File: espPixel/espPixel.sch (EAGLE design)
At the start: 83 parts, among them IC1 74LVC1T45GW,125, IC2 74LVC1T45GW,125, IC3 MP2315GJ-Z, IC4 CP2104, J1 TBLH10-350-04BK, J2 TBLH10-350-03BK, J3 TBLH10-350-02BK, Q1 SIR414DP-T1-GE3, Q2 SIR414DP-T1-GE3, Q5 mmbt2222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

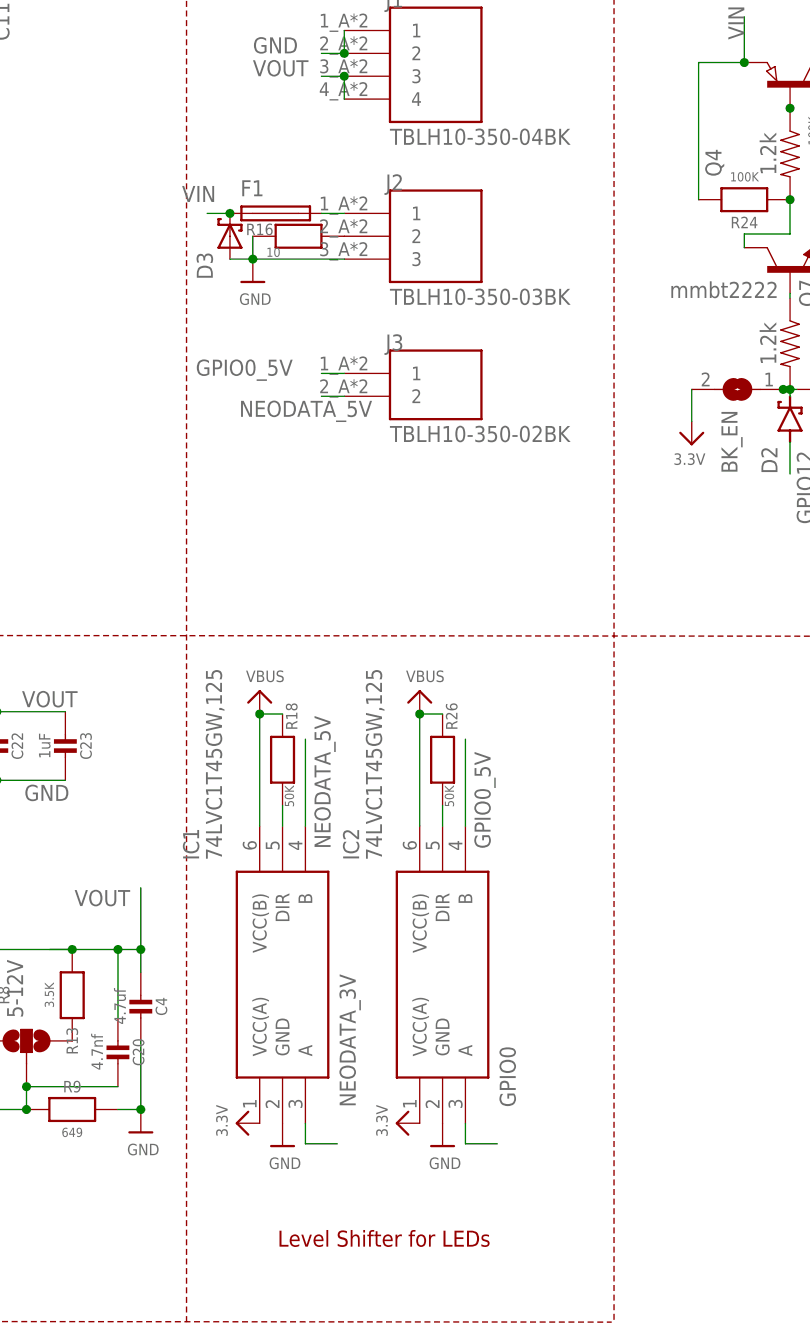
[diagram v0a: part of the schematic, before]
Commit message: v3 more compact size
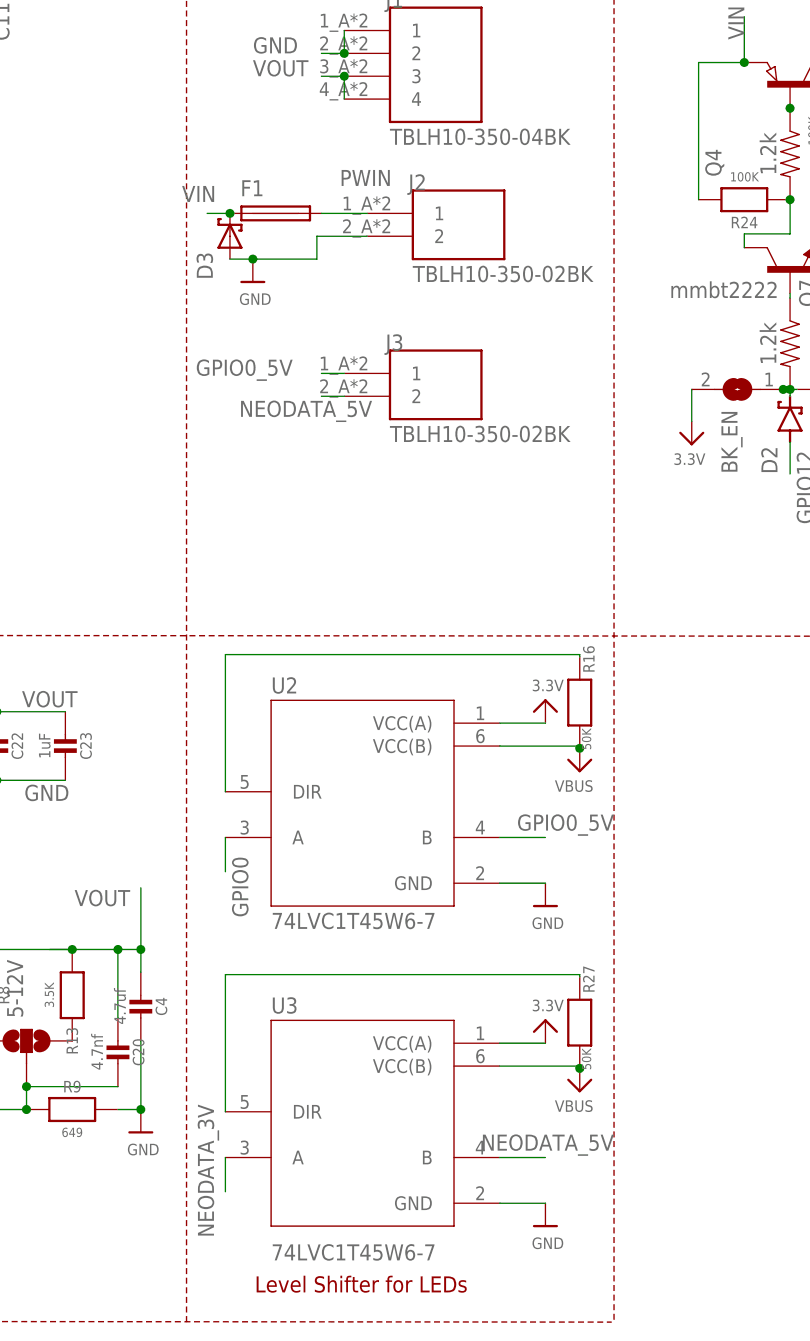
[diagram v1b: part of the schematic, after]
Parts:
- removed IC1, IC2: 74LVC1T45GW,125, 74LVC1T45GW_125:74LVC1T45GW,125
- removed R18, R26: 50K, microbuilder:RESISTOR_0603_NOOUT
- added R27: 50K, microbuilder:RESISTOR_0603_NOOUT
- added U2, U3: 74LVC1T45W6-7, 74LVC1T45W6-7:74LVC1T45W6-7
- J2: value TBLH10-350-03BK -> TBLH10-350-02BK; device TBLH10-350-03BK:TBLH10-350-03BK -> TBLH10-350-02BK:TBLH10-350-02BK
- R16: value 10 -> 50K
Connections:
- net N$20 renamed PWIN
- removed net N$16: IC2.DIR, R26.2
- removed net N$19: J2.2, R16.1
- removed net N$22: IC1.DIR, R18.2
- new net N$10: R27.1, U3.DIR
- new net N$28: R16.1, U2.DIR
- net 3.3V: now also U2.VCC(A), U3.VCC(A); no longer IC1.VCC(A), IC2.VCC(A)
- net GND: now also J2.2, U2.GND, U3.GND; no longer IC1.GND, IC2.GND, J2.3, R16.2
- net GPIO0: now also U2.A; no longer IC2.A
- net GPIO0_5V: now also U2.B; no longer IC2.B
- net NEODATA_3V: now also U3.A; no longer IC1.A
- net NEODATA_5V: now also U3.B; no longer IC1.B
- net VBUS: now also R16.2, R27.2, U2.VCC(B), U3.VCC(B); no longer IC1.VCC(B), IC2.VCC(B), R18.1, R26.1
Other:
- moved on the sheet: R16
